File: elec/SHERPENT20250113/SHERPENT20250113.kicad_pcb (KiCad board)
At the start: 2 copper layers, 1 part

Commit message: Début du layout
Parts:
- removed REF**: ESP32-WROOM-32E, RF_Module:ESP32-WROOM-32E
- added BT1: Battery_Cell, Connector_PinHeader_2.54mm:PinHeader_1x02_P2.54mm_Vertical, F.Cu at (129.0, 90.3)
- added C1: 100nf, Capacitor_SMD:C_0603_1608Metric_Pad1.08x0.95mm_HandSolder, F.Cu at (102.8, 82.6)
- added C10: 22u, Capacitor_SMD:C_0603_1608Metric_Pad1.08x0.95mm_HandSolder, F.Cu at (107.2, 85.1)
- added C11: 22u, Capacitor_SMD:C_0603_1608Metric_Pad1.08x0.95mm_HandSolder, F.Cu at (107.2, 87.6)
- added C12: 22u, Capacitor_SMD:C_0603_1608Metric_Pad1.08x0.95mm_HandSolder, F.Cu at (107.2, 90.1)
- added C13: 100n, Capacitor_SMD:C_0603_1608Metric_Pad1.08x0.95mm_HandSolder, F.Cu at (222.2, 106.5)
- added C14: 100n, Capacitor_SMD:C_0603_1608Metric_Pad1.08x0.95mm_HandSolder, F.Cu at (218.7, 106.6)
- added C15: 1.8p, Capacitor_SMD:C_0402_1005Metric_Pad0.74x0.62mm_HandSolder, F.Cu at (216.1, 99.4)
- added C16: 10n, Capacitor_SMD:C_0603_1608Metric_Pad1.08x0.95mm_HandSolder, F.Cu at (214.8, 96.6)
- added C17: 1u, Capacitor_SMD:C_0603_1608Metric_Pad1.08x0.95mm_HandSolder, F.Cu at (216.3, 96.6)
- added C18: 10u, Capacitor_SMD:C_0402_1005Metric_Pad0.74x0.62mm_HandSolder, F.Cu at (212.8, 101.6)
- added C19: 100n, Capacitor_SMD:C_0402_1005Metric_Pad0.74x0.62mm_HandSolder, F.Cu at (214.4, 102.0)
- added C2: 100n, Capacitor_SMD:C_0603_1608Metric_Pad1.08x0.95mm_HandSolder, F.Cu at (102.8, 85.1)
- added C20: 1u, Capacitor_SMD:C_0402_1005Metric_Pad0.74x0.62mm_HandSolder, F.Cu at (216.1, 101.6)
- added C21: 10nf, Capacitor_SMD:C_0603_1608Metric_Pad1.08x0.95mm_HandSolder, F.Cu at (235.9, 62.2)
- added C22: 15p, Capacitor_SMD:C_0402_1005Metric_Pad0.74x0.62mm_HandSolder, F.Cu at (218.2, 95.3)
- added C23: 15p, Capacitor_SMD:C_0402_1005Metric_Pad0.74x0.62mm_HandSolder, F.Cu at (220.8, 95.8)
- added C24: 1u, Capacitor_SMD:C_0603_1608Metric_Pad1.08x0.95mm_HandSolder, F.Cu at (226.0, 107.1)
- added C25: TBD, Capacitor_SMD:C_0603_1608Metric_Pad1.08x0.95mm_HandSolder, F.Cu at (111.5, 90.1)
- added C3: 2.2u, Capacitor_SMD:C_0603_1608Metric_Pad1.08x0.95mm_HandSolder, F.Cu at (102.8, 87.6)
- added C4: 39n, Capacitor_SMD:C_0603_1608Metric_Pad1.08x0.95mm_HandSolder, F.Cu at (102.8, 90.1)
- added C5: 91p, Capacitor_SMD:C_0603_1608Metric_Pad1.08x0.95mm_HandSolder, F.Cu at (102.8, 92.6)
- added C6: 47u, Capacitor_SMD:C_0603_1608Metric_Pad1.08x0.95mm_HandSolder, F.Cu at (102.8, 95.1)
- added C7: 10u, Capacitor_SMD:C_0603_1608Metric_Pad1.08x0.95mm_HandSolder, F.Cu at (102.8, 97.6)
- added C8: 1.8p, Capacitor_SMD:C_0402_1005Metric_Pad0.74x0.62mm_HandSolder, F.Cu at (212.8, 99.4)
- added C9: 22u, Capacitor_SMD:C_0603_1608Metric_Pad1.08x0.95mm_HandSolder, F.Cu at (107.2, 82.6)
- added D1: LED, LED_SMD:LED_0603_1608Metric_Pad1.05x0.95mm_HandSolder, F.Cu at (97.8, 92.0)
- added D2: D_Schottky, LED_SMD:LED_0603_1608Metric_Pad1.05x0.95mm_HandSolder, F.Cu at (252.4, 87.6)
- added D3: LED, LED_SMD:LED_0603_1608Metric_Pad1.05x0.95mm_HandSolder, F.Cu at (223.7, 110.6)
- added F1: 10A, Fuse:Fuse_0603_1608Metric, F.Cu at (102.6, 62.5)
- added J1: 2137160001, 2137160001:MOLEX_2137160001, F.Cu at (122.5, 71.8)
- added L1: 1.2u, Inductor_SMD:L_0603_1608Metric, F.Cu at (102.6, 65.0)
- added L2: 2.7n, Inductor_SMD:L_0402_1005Metric_Pad0.77x0.64mm_HandSolder, F.Cu at (214.5, 100.0)
- added L3: 2n, Inductor_SMD:L_0402_1005Metric_Pad0.77x0.64mm_HandSolder, F.Cu at (214.5, 101.0)
- added Q1: NMOS, Package_TO_SOT_SMD:SOT-23, F.Cu at (98.0, 83.8)
- added Q2: PMOS, Package_TO_SOT_SMD:SOT-23, F.Cu at (98.0, 88.5)
- added R1: 51.1k, Resistor_SMD:R_0603_1608Metric, F.Cu at (102.6, 72.5)
- added R10: 10k, Resistor_SMD:R_0603_1608Metric, F.Cu at (106.7, 75.0)
- added R11: 10k, Resistor_SMD:R_0603_1608Metric, F.Cu at (231.1, 54.6)
- added R12: 0, Resistor_SMD:R_0603_1608Metric, F.Cu at (231.1, 57.1)
- added R13: 10k, Resistor_SMD:R_0603_1608Metric, F.Cu at (235.1, 39.6)
- added R14: 0, Resistor_SMD:R_0603_1608Metric, F.Cu at (235.1, 42.1)
- added R15: 10k, Resistor_SMD:R_0603_1608Metric, F.Cu at (235.1, 44.6)
- added R16: 0, Resistor_SMD:R_0603_1608Metric, F.Cu at (235.1, 47.1)
- added R17: 10k, Resistor_SMD:R_0603_1608Metric, F.Cu at (235.1, 49.6)
- added R18: 130, Resistor_SMD:R_0603_1608Metric, F.Cu at (221.2, 109.8)
- added R19: 0, Resistor_SMD:R_0402_1005Metric_Pad0.72x0.64mm_HandSolder, F.Cu at (218.3, 97.6)
- added R2: 48.7k, Resistor_SMD:R_0603_1608Metric, F.Cu at (102.6, 75.0)
- added R20: 10k, Resistor_SMD:R_0603_1608Metric, F.Cu at (235.1, 54.6)
- added R21: 10k, Resistor_SMD:R_0603_1608Metric, F.Cu at (229.0, 101.9)
- added R22: 10k, Resistor_SMD:R_0603_1608Metric, F.Cu at (114.7, 62.5)
- added R23: 0, Resistor_SMD:R_0603_1608Metric, F.Cu at (114.7, 65.0)
- added R24: 10k, Resistor_SMD:R_0603_1608Metric, F.Cu at (114.7, 67.5)
- added R25: 0, Resistor_SMD:R_0603_1608Metric, F.Cu at (114.7, 70.0)
- added R3: 523k, Resistor_SMD:R_0603_1608Metric, F.Cu at (102.6, 77.6)
- added R4: 0, Resistor_SMD:R_0603_1608Metric, F.Cu at (102.6, 80.1)
- added R5: 36k, Resistor_SMD:R_0603_1608Metric, F.Cu at (106.7, 62.5)
- added R6: 36k, Resistor_SMD:R_0603_1608Metric, F.Cu at (106.7, 65.0)
- added R7: 100k, Resistor_SMD:R_0603_1608Metric, F.Cu at (106.7, 67.5)
- added R8: 36k, Resistor_SMD:R_0603_1608Metric, F.Cu at (106.7, 70.0)
- added R9: 2k, Resistor_SMD:R_0603_1608Metric, F.Cu at (106.7, 72.5)
- added SW1: SW_Push, CS1213AGF160:SW_CS1213AG_CRS, F.Cu at (254.0, 69.4)
- added TP1: TestPoint, TestPoint:TestPoint_Loop_D2.54mm_Drill1.5mm_Beaded, F.Cu at (150.5, 61.5)
- added TP2: TestPoint, TestPoint:TestPoint_Loop_D2.54mm_Drill1.5mm_Beaded, F.Cu at (150.5, 66.5)
- added TP3: TestPoint, TestPoint:TestPoint_Loop_D2.54mm_Drill1.5mm_Beaded, F.Cu at (220.5, 35.0)
- added TP4: TestPoint, TestPoint:TestPoint_Loop_D2.54mm_Drill1.5mm_Beaded, F.Cu at (220.5, 40.0)
- added TP5: TestPoint, TestPoint:TestPoint_Loop_D2.54mm_Drill1.5mm_Beaded, F.Cu at (205.5, 58.6)
- added TP6: TestPoint, TestPoint:TestPoint_Loop_D2.54mm_Drill1.5mm_Beaded, F.Cu at (205.5, 63.7)
- added TP7: TestPoint, TestPoint:TestPoint_Loop_D2.54mm_Drill1.5mm_Beaded, F.Cu at (150.5, 71.6)
- added TP8: TestPoint, TestPoint:TestPoint_Loop_D2.54mm_Drill1.5mm_Beaded, F.Cu at (150.5, 76.6)
- added TP9: TestPoint, TestPoint:TestPoint_Loop_D2.54mm_Drill1.5mm_Beaded, F.Cu at (150.5, 81.7)
- added U1: AN034_ANTENNA, AN034_ANTENNA:AN034_ANTENNA, F.Cu at (211.9, 105.0)
- added U2: MCP73831T-2ACI_OT, MCP73831T_2ACI_OT:SOT95P280X145-5N, F.Cu at (126.3, 79.0)
- added U3: TPS61288LRQQR, TPS61288LRQQR:RQQ0011A-MFG, F.Cu at (126.9, 74.9)
- added U4: TPS7A2633DRVR, TPS7A2633DRVR:SON65P200X200X80-7N, F.Cu at (131.7, 74.7)
- added U5: LM66200DRLR, LM66200DRLR:SOT-5X3_DRL_TEX-L, F.Cu at (131.4, 78.3)
- added U6: ESP32-C3, ESP32_C3:QFN32_5X5_EXP-L, F.Cu at (219.5, 101.9)
- added U7: W25Q128JVS, W25Q128JVSIQ:SOIC_128JVSIQ_WIN-L, F.Cu at (225.3, 101.9)
- added Y1: 40MHz, 830059627:SMD_059627_WRE-L, F.Cu at (219.5, 96.7)

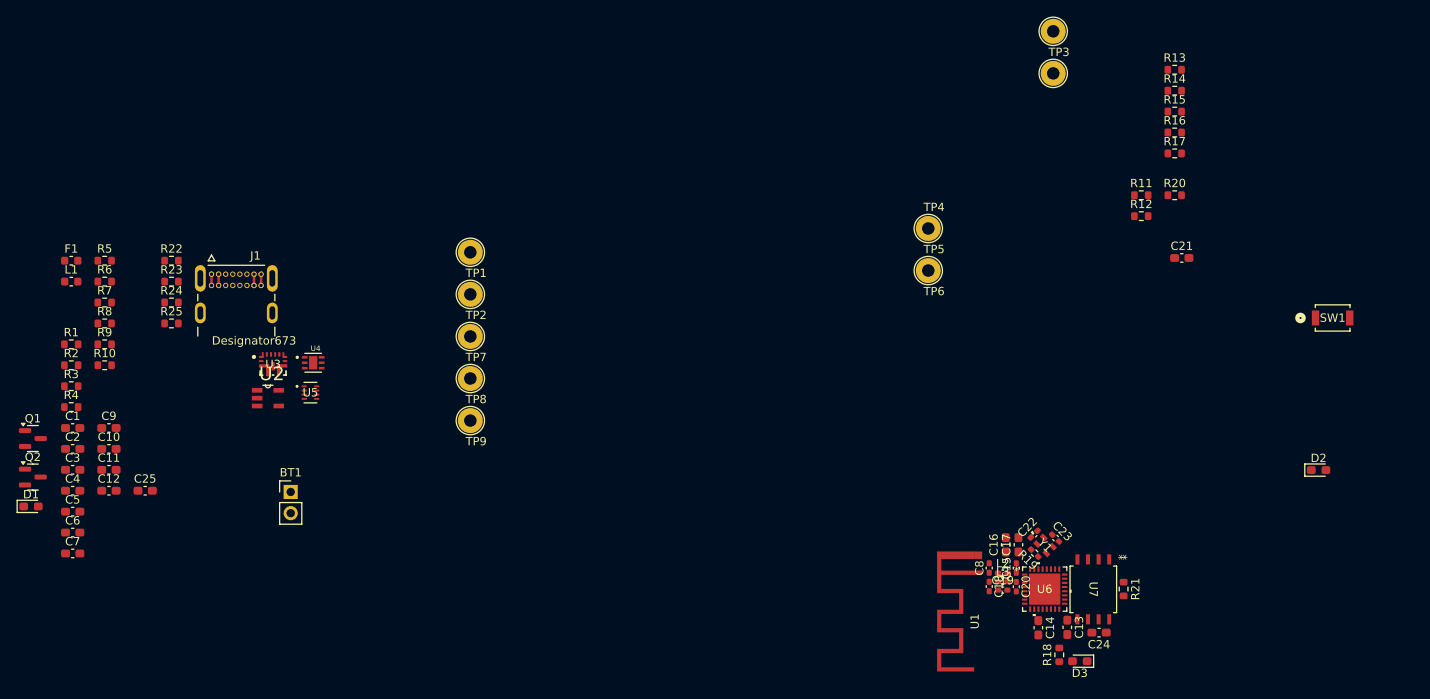
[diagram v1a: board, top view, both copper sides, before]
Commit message: Layout: circuit ESP finalisé + début du circuit buck-boost
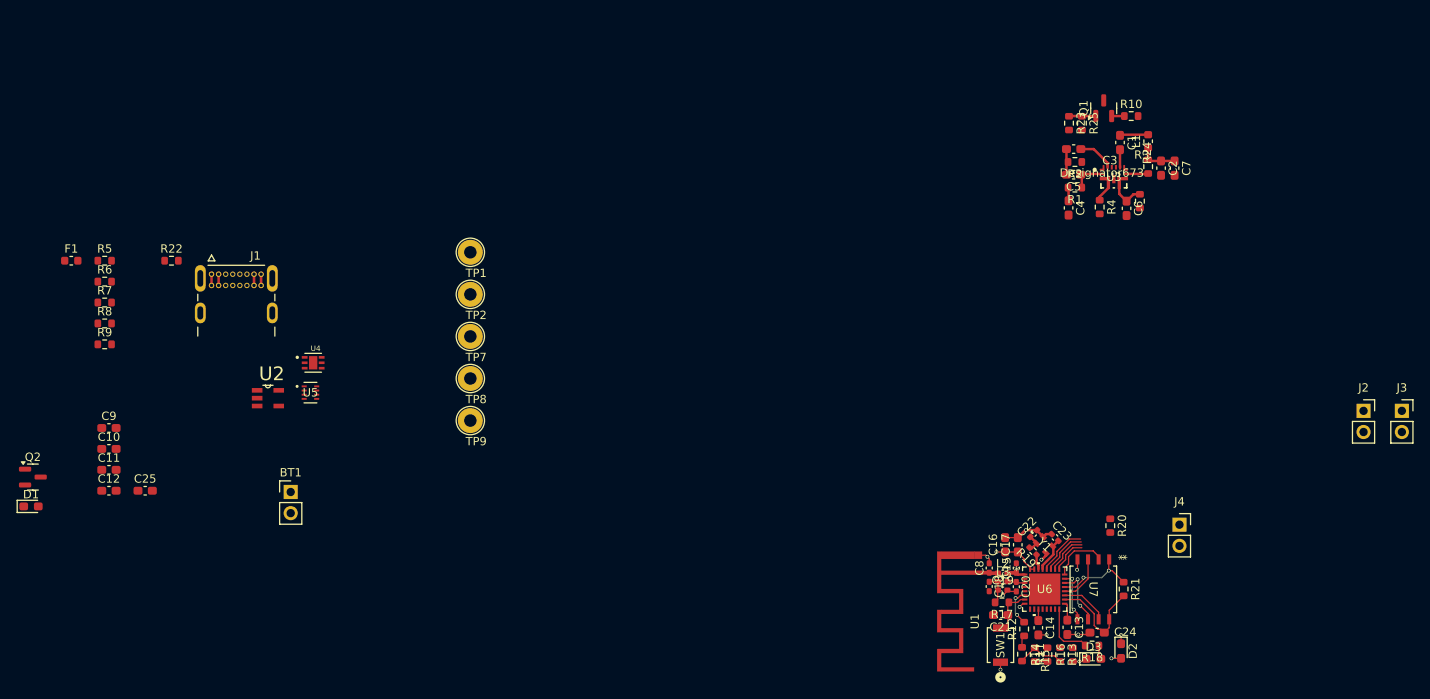
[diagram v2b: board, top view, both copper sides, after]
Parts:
- removed TP3, TP4, TP5, TP6: TestPoint, TestPoint:TestPoint_Loop_D2.54mm_Drill1.5mm_Beaded
- added J2: Conn_01x02_Socket, Connector_PinSocket_2.54mm:PinSocket_1x02_P2.54mm_Vertical, F.Cu at (257.8, 80.5)
- added J3: Conn_01x02_Socket, Connector_PinSocket_2.54mm:PinSocket_1x02_P2.54mm_Vertical, F.Cu at (262.4, 80.5)
- added J4: Conn_01x02_Socket, Connector_PinSocket_2.54mm:PinSocket_1x02_P2.54mm_Vertical, F.Cu at (235.7, 94.2)
- moved C7 140.1 mm to (235.1, 51.4), turned to -90 degrees
- moved C2 134.9 mm to (233.5, 51.4), turned to -90 degrees
- moved Q1 134.5 mm to (226.6, 44.2), turned to 90 degrees
- moved C6 132.3 mm to (229.3, 56.2), turned to -90 degrees
- moved L1 130.4 mm to (231.9, 48.2), turned to 90 degrees
- moved C1 130.3 mm to (228.5, 48.3), turned to -90 degrees
- moved R3 130.2 mm to (230.9, 55.3), turned to -90 degrees
- moved R10 126.8 mm to (229.9, 45.1)
- moved C5 126.8 mm to (223.0, 52.2), turned to 180 degrees
- moved C3 126.2 mm to (223.0, 49.1), turned to 180 degrees
- moved R4 125.8 mm to (226.1, 56.1), turned to -90 degrees
- moved C4 124.3 mm to (222.4, 56.2), turned to -90 degrees
- moved R2 122.9 mm to (223.1, 50.6), turned to 180 degrees
- moved R1 121.9 mm to (223.1, 53.7), turned to 180 degrees
- moved R24 118.4 mm to (231.9, 51.2), turned to -90 degrees
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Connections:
- U6 pad 12: unconnected-(U6-MTCK-Pad12) -> Net-(J3-Pin_2)
- U6 pad 13: unconnected-(U6-MTDO-Pad13) -> Net-(J3-Pin_1)
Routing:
- net GND: track 0.00 -> 23.6 mm, vias 0 -> 10
- net +3.3V: track 0.00 -> 20.0 mm, vias 0 -> 2
- net SQPI_VDD_ESP: track 0.00 -> 12.8 mm
- net SQPI_SS_ESP: track 0.00 -> 9.95 mm, vias 0 -> 2
- net SQPI_SCLK_ESP: track 0.00 -> 7.06 mm, vias 0 -> 2
- net Net-(U6-GPIO10): track 0.00 -> 6.92 mm
- net SQPI_SD0_ESP: track 0.00 -> 6.87 mm
- net Net-(U6-CHIP_EN): track 0.00 -> 6.25 mm
- net U0TXD: track 0.00 -> 6.10 mm
- net SQPI_SD1_ESP: track 0.00 -> 6.05 mm, vias 0 -> 2
- net SQPI_SD2_ESP: track 0.00 -> 5.75 mm
- net SQPI_SD3_ESP: track 0.00 -> 5.75 mm
- net U0RXD: track 0.00 -> 5.53 mm
- net USB_ESP32P: track 0.00 -> 4.97 mm
- net VBATT: track 0.00 -> 4.67 mm
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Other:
- copper layers 2 -> 4

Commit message: Added pcb outline and gitignore
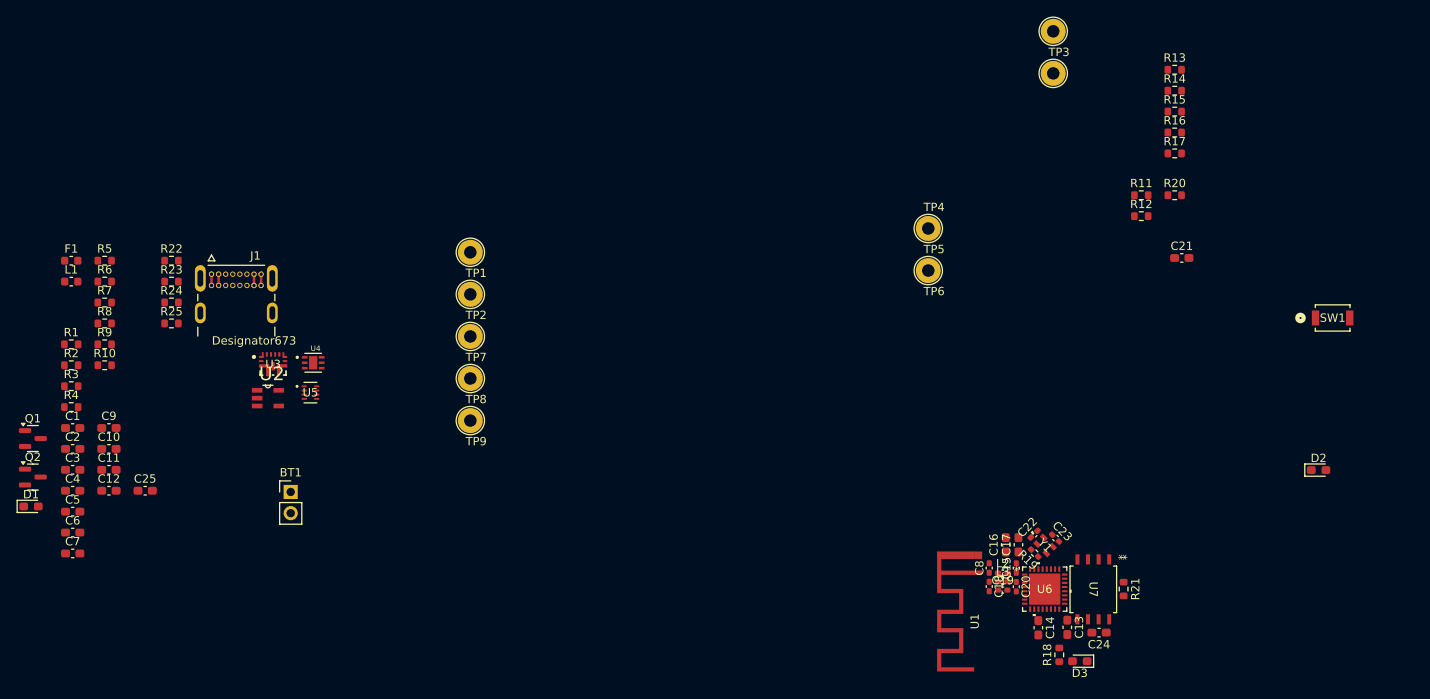
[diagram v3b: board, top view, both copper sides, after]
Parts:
- removed J2, J3, J4: Conn_01x02_Socket, Connector_PinSocket_2.54mm:PinSocket_1x02_P2.54mm_Vertical
- added TP3: TestPoint, TestPoint:TestPoint_Loop_D2.54mm_Drill1.5mm_Beaded, F.Cu at (220.5, 35.0)
- added TP4: TestPoint, TestPoint:TestPoint_Loop_D2.54mm_Drill1.5mm_Beaded, F.Cu at (220.5, 40.0)
- added TP5: TestPoint, TestPoint:TestPoint_Loop_D2.54mm_Drill1.5mm_Beaded, F.Cu at (205.5, 58.6)
- added TP6: TestPoint, TestPoint:TestPoint_Loop_D2.54mm_Drill1.5mm_Beaded, F.Cu at (205.5, 63.7)
- moved C7 140.1 mm to (102.8, 97.6), turned to 0 degrees
- moved C2 134.9 mm to (102.8, 85.1), turned to 0 degrees
- moved Q1 134.5 mm to (98.0, 83.8), turned to 0 degrees
- moved C6 132.3 mm to (102.8, 95.1), turned to 0 degrees
- moved L1 130.4 mm to (102.6, 65.0), turned to 0 degrees
- moved C1 130.3 mm to (102.8, 82.6), turned to 0 degrees
- moved R3 130.2 mm to (102.6, 77.6), turned to 0 degrees
- moved R10 126.8 mm to (106.7, 75.0)
- moved C5 126.8 mm to (102.8, 92.6), turned to 0 degrees
- moved C3 126.2 mm to (102.8, 87.6), turned to 0 degrees
- moved R4 125.8 mm to (102.6, 80.1), turned to 0 degrees
- moved C4 124.3 mm to (102.8, 90.1), turned to 0 degrees
- moved R2 122.9 mm to (102.6, 75.0), turned to 0 degrees
- moved R1 121.9 mm to (102.6, 72.5), turned to 0 degrees
- moved R24 118.4 mm to (114.7, 67.5), turned to 0 degrees
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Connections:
- U6 pad 12: Net-(J3-Pin_2) -> unconnected-(U6-MTCK-Pad12)
- U6 pad 13: Net-(J3-Pin_1) -> unconnected-(U6-MTDO-Pad13)
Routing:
- net GND: track 23.6 -> 0.00 mm, vias 10 -> 0
- net +3.3V: track 20.0 -> 0.00 mm, vias 2 -> 0
- net SQPI_VDD_ESP: track 12.8 -> 0.00 mm
- net SQPI_SS_ESP: track 9.95 -> 0.00 mm, vias 2 -> 0
- net SQPI_SCLK_ESP: track 7.06 -> 0.00 mm, vias 2 -> 0
- net Net-(U6-GPIO10): track 6.92 -> 0.00 mm
- net SQPI_SD0_ESP: track 6.87 -> 0.00 mm
- net Net-(U6-CHIP_EN): track 6.25 -> 0.00 mm
- net U0TXD: track 6.10 -> 0.00 mm
- net SQPI_SD1_ESP: track 6.05 -> 0.00 mm, vias 2 -> 0
- net SQPI_SD2_ESP: track 5.75 -> 0.00 mm
- net SQPI_SD3_ESP: track 5.75 -> 0.00 mm
- net U0RXD: track 5.53 -> 0.00 mm
- net USB_ESP32P: track 4.97 -> 0.00 mm
- net VBATT: track 4.67 -> 0.00 mm
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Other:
- copper layers 4 -> 2

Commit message: fini pour ajd
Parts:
- added D10: WS2812B, LED_SMD:LED_WS2812B_PLCC4_5.0x5.0mm_P3.2mm, F.Cu at (81.0, 150.0)
- added D11: WS2812B, LED_SMD:LED_WS2812B_PLCC4_5.0x5.0mm_P3.2mm, F.Cu at (81.0, 156.6)
- added D12: WS2812B4020, Library:WS2812B4020, F.Cu at (87.7, 141.5)
- added D13: WS2812B4020, Library:WS2812B4020, F.Cu at (87.7, 145.7)
- added D14: WS2812B4020, Library:WS2812B4020, F.Cu at (87.7, 149.9)
- added D15: WS2812B4020, Library:WS2812B4020, F.Cu at (87.7, 154.1)
- added D16: WS2812B4020, Library:WS2812B4020, F.Cu at (87.7, 158.3)
- added D17: WS2812B4020, Library:WS2812B4020, F.Cu at (93.1, 141.5)
- added D18: WS2812B4020, Library:WS2812B4020, F.Cu at (93.1, 145.7)
- added D19: WS2812B4020, Library:WS2812B4020, F.Cu at (93.1, 149.9)
- added D4: WS2812B, LED_SMD:LED_WS2812B_PLCC4_5.0x5.0mm_P3.2mm, F.Cu at (72.9, 143.4)
- added D5: WS2812B, LED_SMD:LED_WS2812B_PLCC4_5.0x5.0mm_P3.2mm, F.Cu at (72.9, 150.0)
- added D6: WS2812B, LED_SMD:LED_WS2812B_PLCC4_5.0x5.0mm_P3.2mm, F.Cu at (72.9, 156.6)
- added D7: WS2812B, LED_SMD:LED_WS2812B_PLCC4_5.0x5.0mm_P3.2mm, F.Cu at (72.9, 163.2)
- added D8: WS2812B, LED_SMD:LED_WS2812B_PLCC4_5.0x5.0mm_P3.2mm, F.Cu at (72.9, 169.9)
- added D9: WS2812B, LED_SMD:LED_WS2812B_PLCC4_5.0x5.0mm_P3.2mm, F.Cu at (81.0, 143.4)
- added J2: Conn_01x02_Socket, Connector_PinSocket_2.54mm:PinSocket_1x02_P2.54mm_Vertical, F.Cu at (87.4, 163.5)
- added J3: Conn_01x02_Socket, Connector_PinSocket_2.54mm:PinSocket_1x02_P2.54mm_Vertical, F.Cu at (92.0, 163.5)
- added TP10: TestPoint, TestPoint:TestPoint_Pad_D1.5mm, F.Cu at (86.8, 170.1)
- moved C14 48.5 mm to (200.7, 151.6)
- moved C15 48.5 mm to (198.1, 144.5)
- moved C18 48.5 mm to (194.8, 146.7)
- moved L2 48.5 mm to (196.5, 145.1)
- moved R21 48.5 mm to (211.0, 147.0)
- moved C22 48.5 mm to (200.2, 140.4)
- moved C20 48.5 mm to (198.1, 146.7)
- moved C8 48.5 mm to (194.8, 144.5)
- moved D3 48.5 mm to (205.7, 155.6)
- moved L3 48.5 mm to (196.5, 146.1)
- moved R18 48.5 mm to (203.2, 154.9)
- moved R19 48.5 mm to (200.3, 142.7)
- moved U1 48.5 mm to (193.9, 150.1)
- moved U6 48.5 mm to (201.5, 147.0)
- moved U7 48.5 mm to (207.3, 147.0)
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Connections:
- TP4 pad 1: USB_ESP32N -> unconnected-(TP4-Pad1)
- U6 pad 12: unconnected-(U6-MTCK-Pad12) -> Net-(J3-Pin_2)
- U6 pad 13: unconnected-(U6-MTDO-Pad13) -> Net-(J3-Pin_1)
- U6 pad 25: USB_ESP32N -> unconnected-(U6-GPIO18-Pad25)

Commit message: Avancement du circuit des batteries et de contrôle
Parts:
- removed TP3, TP6: TestPoint, TestPoint:TestPoint_Loop_D2.54mm_Drill1.5mm_Beaded
- added D20: D, Diode_SMD:D_0603_1608Metric_Pad1.05x0.95mm_HandSolder, F.Cu at (152.5, 116.1)
- added J4: Conn_01x03_Socket, Connector_PinSocket_2.54mm:PinSocket_1x03_P2.54mm_Vertical, F.Cu at (196.8, 76.7)
- added R26: 10k, Resistor_SMD:R_0603_1608Metric, F.Cu at (153.2, 84.9)
- J3: value Conn_01x02_Socket -> Conn_01x03_Socket; footprint Connector_PinSocket_2.54mm:PinSocket_1x02_P2.54mm_Vertical -> Connector_PinSocket_2.54mm:PinSocket_1x03_P2.54mm_Vertical
- moved TP4 156.4 mm to (93.1, 130.7)
- moved TP5 136.3 mm to (93.1, 135.8)
- moved D7 127.9 mm to (26.3, 44.1)
- moved D8 127.9 mm to (26.3, 50.7)
- moved D10 127.9 mm to (34.4, 30.9)
- moved D11 127.9 mm to (34.4, 37.5)
- moved D5 127.9 mm to (26.3, 30.9)
- moved D6 127.9 mm to (26.3, 37.5)
- moved D4 127.9 mm to (26.3, 24.2)
- moved D9 127.9 mm to (34.4, 24.2)
- moved D14 126.2 mm to (46.2, 30.8)
- moved D16 126.2 mm to (46.2, 39.2)
- moved D19 126.2 mm to (51.5, 30.8)
- moved D13 126.2 mm to (46.2, 26.6)
- moved D18 126.2 mm to (51.5, 26.6)
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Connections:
- net Net-(J3-Pin_2) renamed /Moteur1_PWM
- net SQPI_SCLK_ESP renamed /SQPI_SCLK_ESP
- net SQPI_SD0_ESP renamed /SQPI_SD0_ESP
- net SQPI_SD1_ESP renamed /SQPI_SD1_ESP
- net SQPI_SD2_ESP renamed /SQPI_SD2_ESP
- net SQPI_SD3_ESP renamed /SQPI_SD3_ESP
- net SQPI_SS_ESP renamed /SQPI_SS_ESP
- net SQPI_VDD_ESP renamed /SQPI_VDD_ESP
- net StayOn renamed /StayOn
- net U0RXD renamed /I2C_DO
- net USB_ESP32P renamed /USB_ESP32P
- net VUSB renamed /VUSB
- C25 pad 1: DIODE_STATE -> /VDIODE
- C9 pad 1: DIODE_STATE -> /VDIODE
- J1 pad A7: USB_ESP32N -> /USB_ESP32N
- J1 pad B7: USB_ESP32N -> /USB_ESP32N
- J2 pad 1: U0TXD -> /I2C_DI
- J3 pad 1: Net-(J3-Pin_1) -> +9V
- Q2 pad 1: CHARGE -> Net-(Q2-D)
- R22 pad 1: Net-(U5-ST) -> /DIODE_STATE
- R22 pad 2: DIODE_STATE -> +3.3V
- TP5 pad 1: U0TXD -> /U0TXD
- TP7 pad 1: DIODE_STATE -> /VDIODE
- U4 pad 4: DIODE_STATE -> /VDIODE
- U4 pad 6: DIODE_STATE -> /VDIODE
- U5 pad 2: DIODE_STATE -> /VDIODE
- U5 pad 6: +9V -> Net-(D20-K)
- U5 pad 7: DIODE_STATE -> /VDIODE
- U5 pad 8: Net-(U5-ST) -> /DIODE_STATE
- U6 pad 13: Net-(J3-Pin_1) -> /Moteur2_PWM
- U6 pad 25: unconnected-(U6-GPIO18-Pad25) -> /USB_ESP32N
- U6 pad 28: U0TXD -> /I2C_DI
- U6 pad 8: DIODE_STATE -> /DIODE_STATE
- U6 pad 9: CHARGE -> /CHARGE
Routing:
- net GND: track 0.00 -> 76.5 mm, vias 0 -> 26
- net /VUSB: track 0.00 -> 48.2 mm, vias 0 -> 1
- net VBATT: track 0.00 -> 47.7 mm, vias 0 -> 2
- net +3.3V: track 0.00 -> 35.6 mm, vias 0 -> 6
- net +9V: track 0.00 -> 24.2 mm
- net /StayOn: track 0.00 -> 21.2 mm, vias 0 -> 2
- net /DIODE_STATE: track 0.00 -> 20.1 mm, vias 0 -> 2
- net /USB_ESP32N: track 0.00 -> 17.7 mm, vias 0 -> 2
- net /USB_ESP32P: track 0.00 -> 17.5 mm, vias 0 -> 2
- net /CHARGE: track 0.00 -> 14.9 mm, vias 0 -> 2
- net Net-(U3-PGND): track 0.00 -> 13.5 mm
- net Net-(U3-FB): track 0.00 -> 13.4 mm, vias 0 -> 2
- net /SQPI_VDD_ESP: track 0.00 -> 12.8 mm
- net Net-(U3-EN): track 0.00 -> 11.6 mm, vias 0 -> 2
- net /VDIODE: track 0.00 -> 10.0 mm
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- added copper zone on In2.Cu, net +3.3V
- added copper zone on F.Cu, net /VDIODE
- added copper zone on In1.Cu, net GND
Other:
- copper layers 2 -> 4
